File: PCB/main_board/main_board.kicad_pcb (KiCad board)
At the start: 2 copper layers, 49 parts, among them CN1 XT30PW-M, CN2 XT30PW-M, U1 XT30PW-F, U3 W25N01GVZEIG_C907680, U4 INA226, U5 INA226, U6 RP2040, U7 AZ1117-3.3, X1 X322512MSB4SI

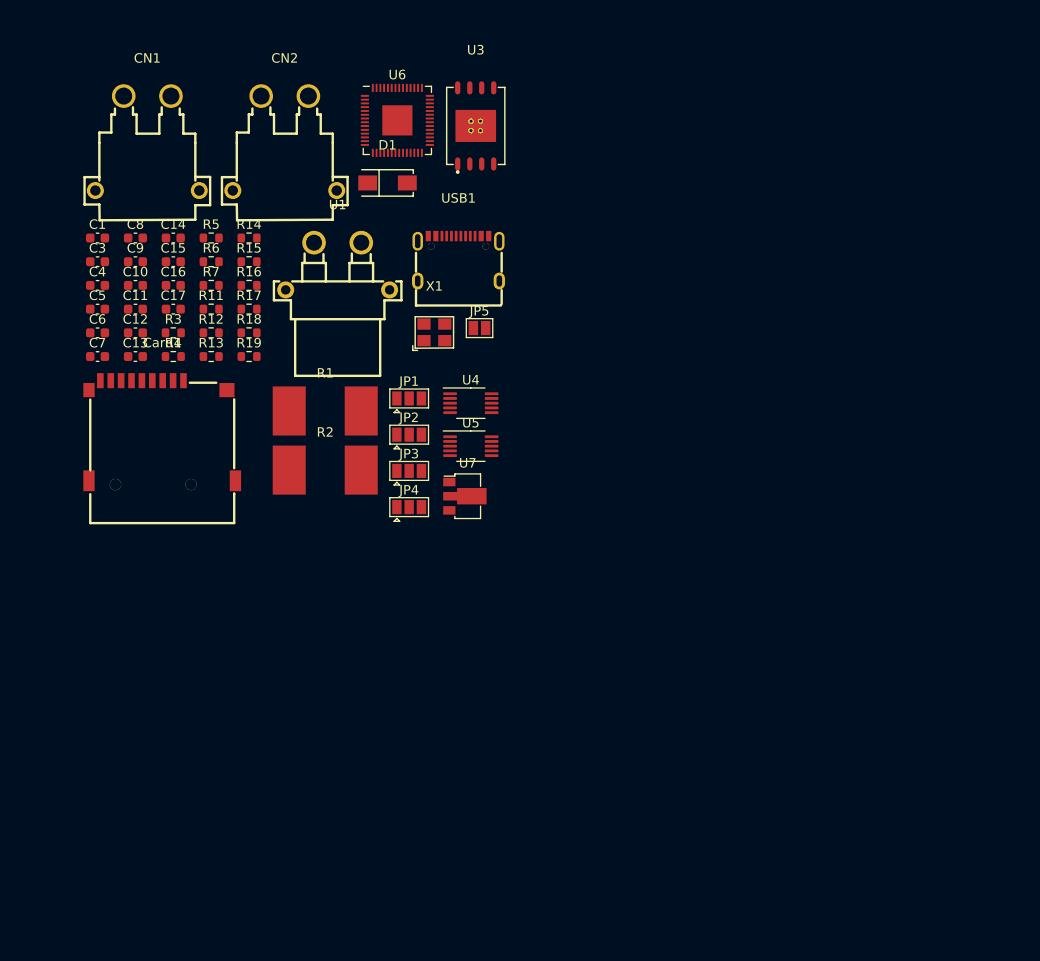
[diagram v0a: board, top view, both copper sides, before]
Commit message: Fundamental pcb layout
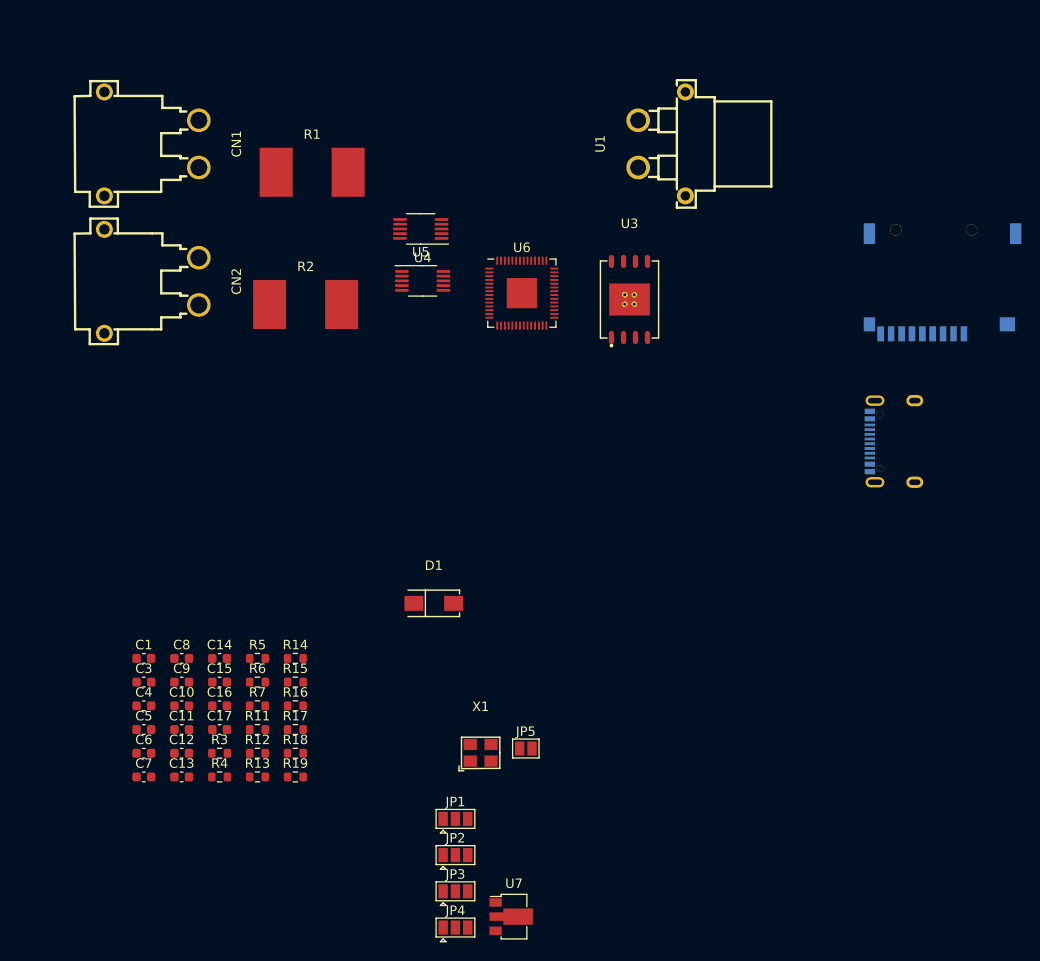
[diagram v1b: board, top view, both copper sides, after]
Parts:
- Card1, USB1: moved to B.Cu
- moved Card1 84.1 mm to (123.2, 46.8)
- moved USB1 49.8 mm to (117.9, 63.5), turned to -90 degrees
- moved C12 44.8 mm to (42.7, 96.5)
- moved C15 44.8 mm to (46.7, 89.0)
- moved C3 44.8 mm to (38.7, 89.0)
- moved C6 44.8 mm to (38.7, 96.5)
- moved C9 44.8 mm to (42.7, 89.0)
- moved JP2 44.8 mm to (71.7, 107.3)
- moved JP4 44.8 mm to (71.7, 115.0)
- moved JP5 44.8 mm to (79.1, 96.0)
- moved R12 44.8 mm to (50.7, 96.5)
- moved R15 44.8 mm to (54.7, 89.0)
- moved R18 44.8 mm to (54.7, 96.5)
- moved R3 44.8 mm to (46.7, 96.5)
- moved R6 44.8 mm to (50.7, 89.0)
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
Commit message: add PCB outline, redesign power component
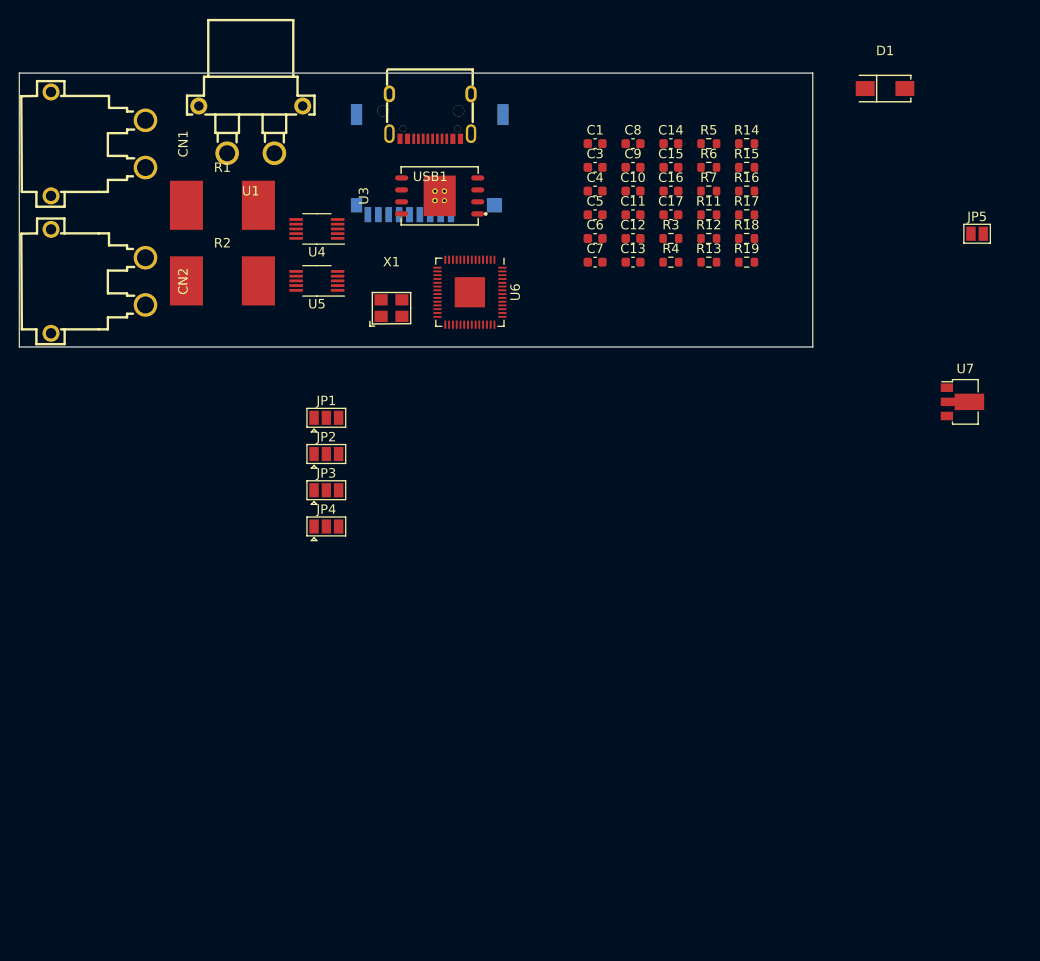
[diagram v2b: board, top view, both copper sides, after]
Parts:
- USB1: moved to F.Cu
- moved C12 72.5 mm to (90.5, 42.0)
- moved C15 72.5 mm to (94.5, 34.5)
- moved C9 72.5 mm to (90.5, 34.5)
- moved JP5 72.5 mm to (126.9, 41.5)
- moved R15 72.5 mm to (102.5, 34.5)
- moved R18 72.5 mm to (102.5, 42.0)
- moved R3 72.5 mm to (94.5, 42.0)
- moved C1 72.5 mm to (86.5, 32.0)
- moved C10 72.5 mm to (90.5, 37.0)
- moved C11 72.5 mm to (90.5, 39.5)
- moved C13 72.5 mm to (90.5, 44.5)
- moved C14 72.5 mm to (94.5, 32.0)
- moved C16 72.5 mm to (94.5, 37.0)
- moved C17 72.5 mm to (94.5, 39.5)
- moved C3 72.5 mm to (86.5, 34.5)
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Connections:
- R5 pad 1: IBAT+ -> ICAP+
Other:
- board outline added: 84 x 29 mm

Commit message: Update main_board.kicad_pcb
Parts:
- JP1, JP2, JP3, JP4: moved to B.Cu
- moved U7 72.2 mm to (58.7, 32.4)
- moved D1 55.0 mm to (63.0, 35.9), turned to 90 degrees
- moved C4 23.1 mm to (68.7, 51.8), turned to -90 degrees
- moved C7 22.9 mm to (63.7, 46.8), turned to 180 degrees
- moved JP3 22.9 mm to (57.0, 45.8), turned to 180 degrees
- moved JP1 22.9 mm to (57.0, 38.2), turned to 180 degrees
- moved JP2 22.9 mm to (57.0, 42.0), turned to 180 degrees
- moved JP4 22.9 mm to (57.0, 49.7), turned to 180 degrees
- moved C8 17.9 mm to (75.4, 41.7)
- moved C5 13.7 mm to (75.7, 48.0), turned to 180 degrees
- moved C6 11.5 mm to (75.7, 46.0)
- moved C11 10.1 mm to (94.0, 49.0)
- moved C12 10.1 mm to (94.0, 51.5)
- moved C13 10.1 mm to (94.0, 54.0)
- moved R11 10.1 mm to (102.0, 49.0)
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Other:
- board size 84 x 29 mm -> 57 x 29 mm

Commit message: basic layout complete
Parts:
- moved C14 23.8 mm to (75.7, 46.6)
- moved C1 2.46 mm to (88.6, 30.8)
- moved C6 0.90 mm to (75.7, 45.1)
- moved C5 0.10 mm to (75.7, 48.1)
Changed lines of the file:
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@@
     (property "ki_keywords" "RP2040 ARM Cortex-M0+ USB")
     (attr smd)
-    (fp_text reference "U6" (at 0 -4.82 90) (layer "F.SilkS")
+    (fp_text reference "U6" (at -4.7 -2.5) (layer "F.SilkS")
         (effects (font (size 1 1) (thickness 0.15)))
     )
@@
   )
   (footprint "Capacitor_SMD:C_0603_1608Metric" (layer "F.Cu")
-    (at 86.46 31.97)
+    (at 88.625 30.8)
     (descr "Capacitor SMD 0603 (1608 Metric), square (rectangular) end terminal, IPC_7351 nominal, (Body size source: IPC-SM-782 page 76, https://www.pcb-3d.com/wordpress/wp-content/uploads/ipc-sm-782a_amendment_1_and_2.pdf), generated with kicad-footprint-generator")
     (tags "capacitor")
@@
     (property "ki_keywords" "capacitor cap")
     (attr smd)
-    (fp_text reference "C7" (at 0 -1.43) (layer "F.SilkS")
+    (fp_text reference "C7" (at 2.575 -0.1) (layer "F.SilkS")
         (effects (font (size 1 1) (thickness 0.15)))
     )
@@
   )
   (footprint "Capacitor_SMD:C_0603_1608Metric" (layer "F.Cu")
-    (at 75.725 46)
+    (at 75.7 45.1)
     (descr "Capacitor SMD 0603 (1608 Metric), square (rectangular) end terminal, IPC_7351 nominal, (Body size source: IPC-SM-782 page 76, https://www.pcb-3d.com/wordpress/wp-content/uploads/ipc-sm-782a_amendment_1_and_2.pdf), generated with kicad-footprint-generator")
     (tags "capacitor")
@@
     (property "ki_keywords" "capacitor cap")
     (attr smd)
-    (fp_text reference "C6" (at 0 -1.43) (layer "F.SilkS")
+    (fp_text reference "C6" (at 2.5 0) (layer "F.SilkS")
         (effects (font (size 1 1) (thickness 0.15)))
     )
@@
   )
   (footprint "Capacitor_SMD:C_0603_1608Metric" (layer "F.Cu")
-    (at 75.7 48 180)
+    (at 75.7 48.1 180)
     (descr "Capacitor SMD 0603 (1608 Metric), square (rectangular) end terminal, IPC_7351 nominal, (Body size source: IPC-SM-782 page 76, https://www.pcb-3d.com/wordpress/wp-content/uploads/ipc-sm-782a_amendment_1_and_2.pdf), generated with kicad-footprint-generator")
     (tags "capacitor")
@@
     (property "ki_keywords" "capacitor cap")
     (attr smd)
-    (fp_text reference "C5" (at 0 -1.43) (layer "F.SilkS")
+    (fp_text reference "C5" (at -2.5 -0.1) (layer "F.SilkS")
         (effects (font (size 1 1) (thickness 0.15)))
     )
@@
   )
   (footprint "Capacitor_SMD:C_0603_1608Metric" (layer "F.Cu")
-    (at 94.48 31.97)
+    (at 75.7 46.6)
     (descr "Capacitor SMD 0603 (1608 Metric), square (rectangular) end terminal, IPC_7351 nominal, (Body size source: IPC-SM-782 page 76, https://www.pcb-3d.com/wordpress/wp-content/uploads/ipc-sm-782a_amendment_1_and_2.pdf), generated with kicad-footprint-generator")
     (tags "capacitor")
@@
     (property "ki_keywords" "capacitor cap")
     (attr smd)
-    (fp_text reference "C14" (at 0 -1.43) (layer "F.SilkS")
-        (effects (font (size 1 1) (thickness 0.15)))
-    )
+    (fp_text reference "C14" (at 3 0) (layer "F.SilkS")
+        (effects (font (size 1 1) (thickness 0.15)))
+    )

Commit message: stage pull
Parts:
- moved C11 30.2 mm to (64.0, 46.0), turned to 180 degrees
- moved C10 23.3 mm to (72.3, 51.8), turned to -90 degrees
- moved C13 21.8 mm to (75.8, 42.1)
- moved C9 20.4 mm to (75.7, 46.6)
- moved C12 19.9 mm to (75.7, 43.6)
- moved C14 13.1 mm to (88.3, 43.0)
- moved C8 7.91 mm to (75.7, 49.6)
- moved U7 3.18 mm to (58.0, 35.5)
- moved R2 1.40 mm to (47.0, 47.9)
- moved U3 1.08 mm to (70.7, 36.7)
- moved C7 0.77 mm to (64.0, 47.5)
- moved R1 0.70 mm to (47.0, 39.2)
